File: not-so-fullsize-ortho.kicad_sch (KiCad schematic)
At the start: 10 parts, among them J3 Conn_01x03, J4 Conn_01x04

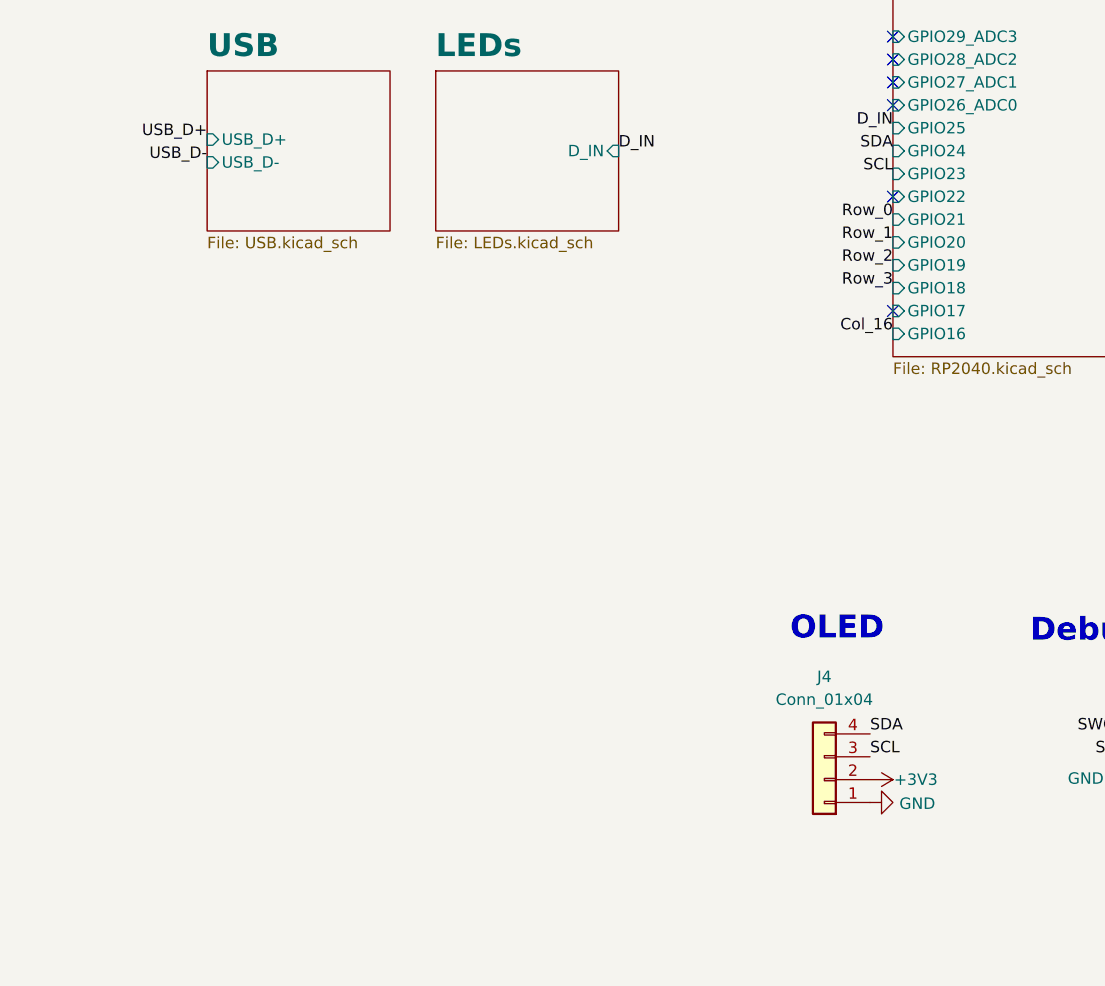
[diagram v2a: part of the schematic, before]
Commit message: remove left most column, reroute rp2040
remove left most column, reroute rp2040 to fit in-between switches, no more oled, last 2 cols (right) are snap off. 
still to do:
- check that the snap cutouts aren't too much,
- add mounting holes for if the side is snapped off.
- still to route columns/rows
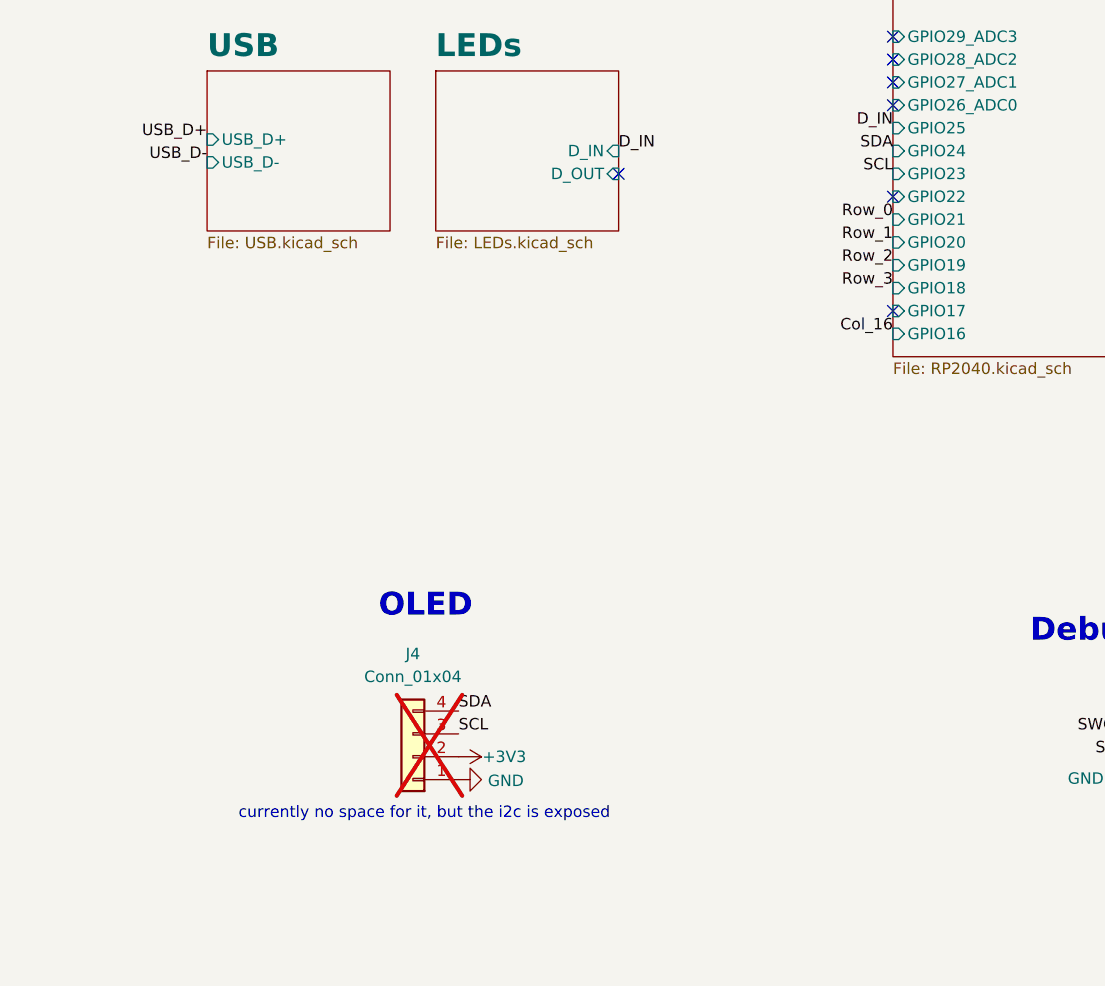
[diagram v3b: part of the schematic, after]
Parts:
- J4: now not fitted
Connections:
- no-connect marks 6 -> 7
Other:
- sheet LEDs ports: added D_OUT; removed none
- note added: "currently no space for it, but the i2c is exposed"
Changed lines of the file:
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@@
+	)
+	(no_connect
+		(at 172.72 151.13)
 	)
 	(no_connect
@@
 		)
 	)
+	(text "currently no space for it, but the i2c is exposed"
+		(exclude_from_sim no)
+		(at 151.13 222.25 0)
+		(effects
+			(font
+				(size 1.27 1.27)
+			)
+		)
+	)
 	(text "OLED"
 		(exclude_from_sim no)
-		(at 191.77 203.2 0)
+		(at 146.05 200.66 0)
 		(effects
 			(font
@@
 	)
 	(label "SCL"
-		(at 200.66 215.9 0)
+		(at 154.94 213.36 0)
 		(fields_autoplaced yes)
 		(effects
@@
 	)
 	(label "SDA"
-		(at 200.66 213.36 0)
+		(at 154.94 210.82 0)
 		(fields_autoplaced yes)
 		(effects
@@
 	(symbol
 		(lib_id "power:GND")
-		(at 200.66 220.98 90)
+		(at 154.94 218.44 90)
 		(mirror x)
 		(unit 1)
@@
 		(dnp no)
 		(property "Reference" "#PWR034"
-			(at 207.01 220.98 0)
+			(at 161.29 218.44 0)
 			(effects
 				(font
@@
 		)
 		(property "Value" "GND"
-			(at 203.9112 221.107 90)
+			(at 158.1912 218.567 90)
 			(effects
 				(font
@@
 		)
 		(property "Footprint" ""
-			(at 200.66 220.98 0)
+			(at 154.94 218.44 0)
 			(effects
 				(font
@@
 		)
 		(property "Datasheet" ""
-			(at 200.66 220.98 0)
+			(at 154.94 218.44 0)
 			(effects
 				(font
@@
 		)
 		(property "Description" ""
-			(at 200.66 220.98 0)
+			(at 154.94 218.44 0)
 			(effects
 				(font
@@
 	(symbol
 		(lib_id "power:+3V3")
-		(at 200.66 218.44 270)
+		(at 154.94 215.9 270)
 		(unit 1)
 		(exclude_from_sim no)
@@
 		(dnp no)
 		(property "Reference" "#PWR035"
-			(at 196.85 218.44 0)
+			(at 151.13 215.9 0)
 			(effects
 				(font
@@
 		)
 		(property "Value" "+3V3"
-			(at 205.74 218.44 90)
+			(at 160.02 215.9 90)
 			(effects
 				(font
@@
 		)
 		(property "Footprint" ""
-			(at 200.66 218.44 0)
+			(at 154.94 215.9 0)
 			(effects
 				(font
@@
 		)
 		(property "Datasheet" ""
-			(at 200.66 218.44 0)
+			(at 154.94 215.9 0)
 			(effects
 				(font
@@
 		)
 		(property "Description" ""
-			(at 200.66 218.44 0)
+			(at 154.94 215.9 0)
 			(effects
 				(font
@@
 	(symbol
 		(lib_id "Connector_Generic:Conn_01x04")
-		(at 195.58 218.44 180)
+		(at 149.86 215.9 180)
 		(unit 1)
 		(exclude_from_sim no)
 		(in_bom yes)
 		(on_board yes)
-		(dnp no)
+		(dnp yes)
 		(fields_autoplaced yes)
 		(property "Reference" "J4"
-			(at 195.58 207.01 0)
+			(at 149.86 204.47 0)
 			(effects
 				(font
@@
 		)
 		(property "Value" "Conn_01x04"
-			(at 195.58 209.55 0)
+			(at 149.86 207.01 0)
 			(effects
 				(font
@@
 		)
 		(property "Footprint" "Connector_PinSocket_2.54mm:PinSocket_1x04_P2.54mm_Vertical"
-			(at 195.58 218.44 0)
+			(at 149.86 215.9 0)
 			(effects
 				(font
@@
 		)
 		(property "Datasheet" "~"
-			(at 195.58 218.44 0)
+			(at 149.86 215.9 0)
 			(effects
 				(font
@@
 		)
 		(property "Description" "Generic connector, single row, 01x04, script generated (kicad-library-utils/schlib/autogen/connector/)"
-			(at 195.58 218.44 0)
+			(at 149.86 215.9 0)
 			(effects
 				(font
@@
 			(effects
 				(font
+					(size 1.27 1.27)
+				)
+				(justify right)
+			)
+		)
+		(pin "D_OUT" input
+			(at 172.72 151.13 0)
+			(effects
+				(font

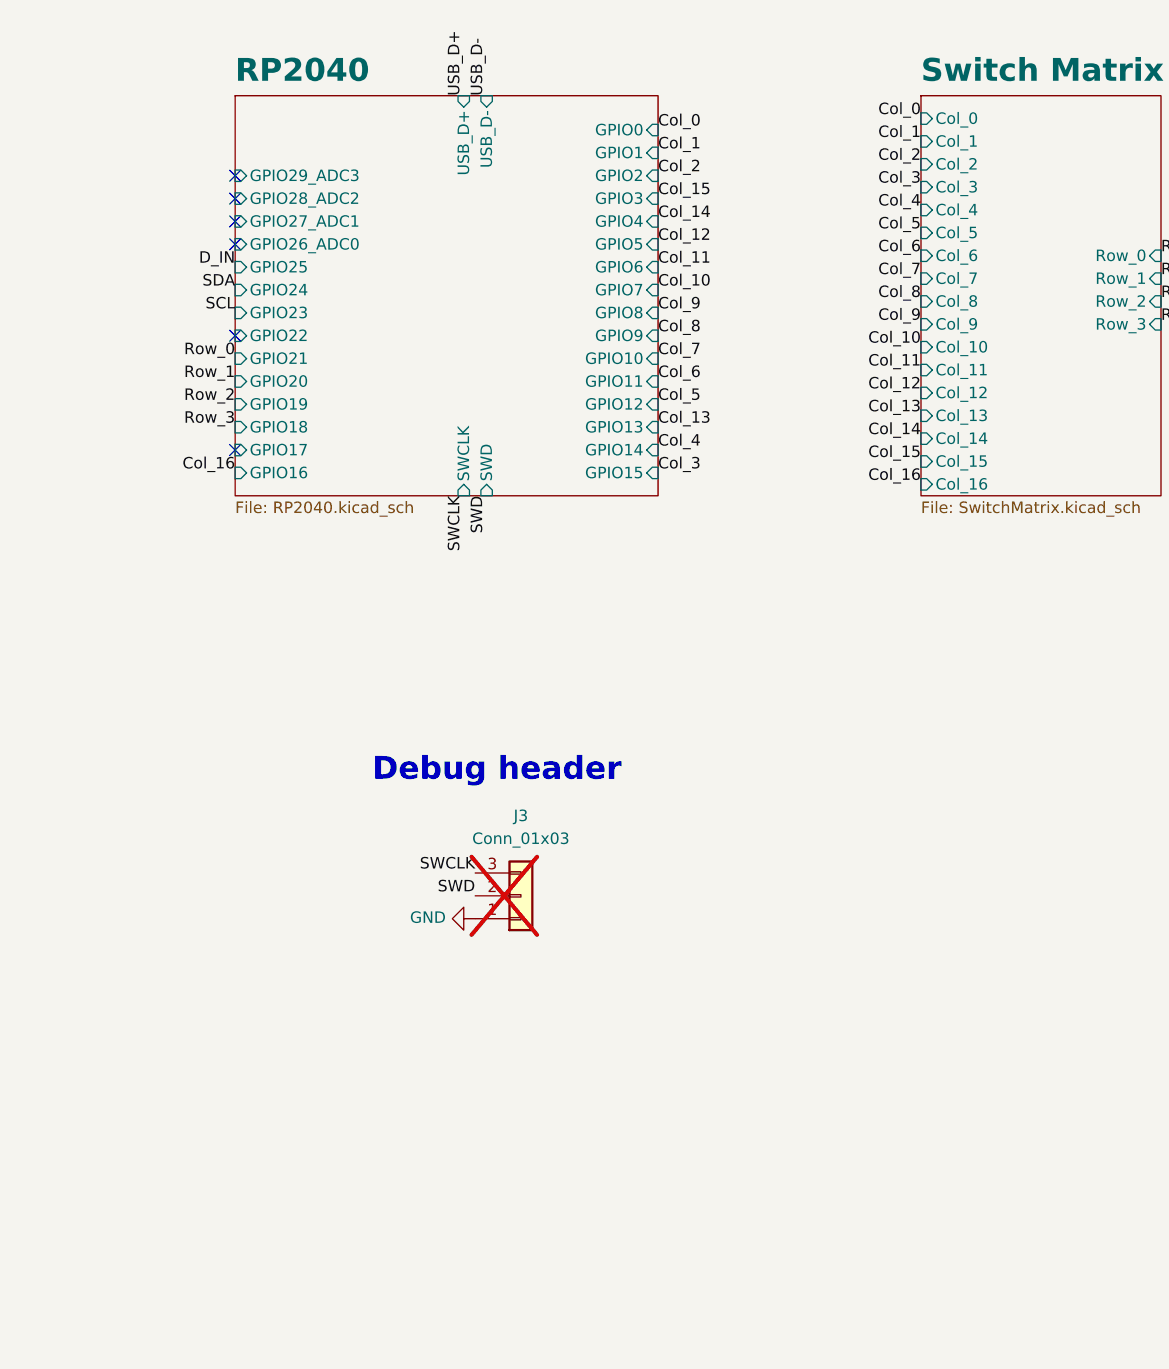
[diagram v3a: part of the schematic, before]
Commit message: routing, rotate leds to make tracks easier
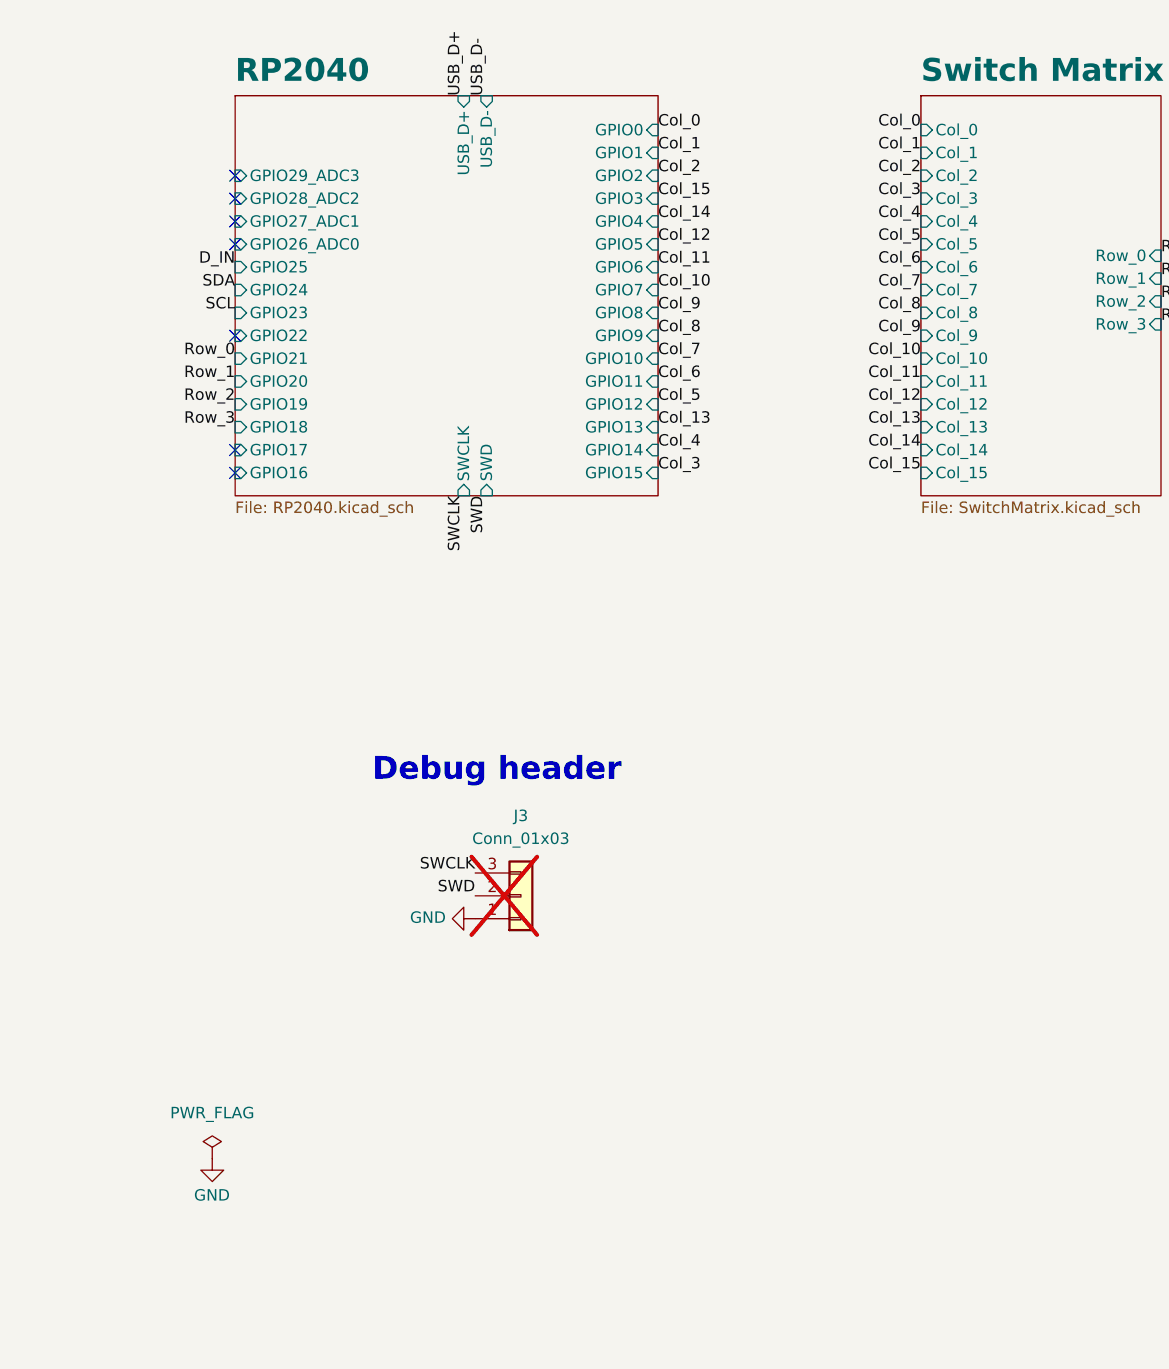
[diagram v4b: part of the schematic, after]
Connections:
- no-connect marks 7 -> 8
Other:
- sheet Switch Matrix ports: added none; removed Col_16
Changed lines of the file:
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@@
+	)
+	(no_connect
+		(at 203.2 168.91)
 	)
 	(no_connect
@@
 	)
 	(label "Col_7"
-		(at 279.4 147.32 180)
-		(fields_autoplaced yes)
-		(effects
-			(font
-				(size 1.27 1.27)
-			)
-			(justify right bottom)
-		)
-	)
-	(label "Col_16"
-		(at 279.4 170.18 180)
+		(at 279.4 148.59 180)
 		(fields_autoplaced yes)
 		(effects
@@
 	)
 	(label "Col_6"
-		(at 279.4 144.78 180)
+		(at 279.4 146.05 180)
 		(fields_autoplaced yes)
 		(effects
@@
 		)
 	)
-	(label "Col_16"
-		(at 203.2 168.91 180)
-		(fields_autoplaced yes)
-		(effects
-			(font
-				(size 1.27 1.27)
-			)
-			(justify right bottom)
-		)
-	)
 	(label "Col_2"
 		(at 250.19 135.89 0)
@@
 	)
 	(label "Col_5"
-		(at 279.4 142.24 180)
+		(at 279.4 143.51 180)
 		(fields_autoplaced yes)
 		(effects
@@
 	)
 	(label "Col_0"
-		(at 279.4 129.54 180)
+		(at 279.4 130.81 180)
 		(fields_autoplaced yes)
 		(effects
@@
 	)
 	(label "Col_4"
-		(at 279.4 139.7 180)
+		(at 279.4 140.97 180)
 		(fields_autoplaced yes)
 		(effects
@@
 	)
 	(label "Col_1"
-		(at 279.4 132.08 180)
+		(at 279.4 133.35 180)
 		(fields_autoplaced yes)
 		(effects
@@
 	)
 	(label "Col_13"
-		(at 279.4 162.56 180)
+		(at 279.4 163.83 180)
 		(fields_autoplaced yes)
 		(effects
@@
 	)
 	(label "Col_15"
-		(at 279.4 167.64 180)
+		(at 279.4 168.91 180)
 		(fields_autoplaced yes)
 		(effects
@@
 	)
 	(label "Col_3"
-		(at 279.4 137.16 180)
+		(at 279.4 138.43 180)
 		(fields_autoplaced yes)
 		(effects
@@
 	)
 	(label "Col_14"
-		(at 279.4 165.1 180)
+		(at 279.4 166.37 180)
 		(fields_autoplaced yes)
 		(effects
@@
 	)
 	(label "Col_9"
-		(at 279.4 152.4 180)
+		(at 279.4 153.67 180)
 		(fields_autoplaced yes)
 		(effects
@@
 	)
 	(label "Col_10"
-		(at 279.4 154.94 180)
+		(at 279.4 156.21 180)
 		(fields_autoplaced yes)
 		(effects
@@
 	)
 	(label "Col_11"
-		(at 279.4 157.48 180)
+		(at 279.4 158.75 180)
 		(fields_autoplaced yes)
 		(effects
@@
 	)
 	(label "Col_8"
-		(at 279.4 149.86 180)
+		(at 279.4 151.13 180)
 		(fields_autoplaced yes)
 		(effects
@@
 	)
 	(label "Col_12"
-		(at 279.4 160.02 180)
+		(at 279.4 161.29 180)
 		(fields_autoplaced yes)
 		(effects
@@
 	)
 	(label "Col_2"
-		(at 279.4 134.62 180)
+		(at 279.4 135.89 180)
 		(fields_autoplaced yes)
 		(effects
@@
 				(path "/e63e39d7-6ac0-4ffd-8aa3-1841a4541b55"
 					(reference "H6")
+					(unit 1)
+				)
+			)
+		)
+	)
+	(symbol
+		(lib_id "PCM_4ms_Power-symbol:PWR_FLAG")
+		(at 200.66 245.11 0)
+		(unit 1)
+		(exclude_from_sim no)
+		(in_bom yes)
+		(on_board yes)
+		(dnp no)
+		(fields_autoplaced yes)
+		(property "Reference" "#FLG02"
+			(at 200.66 243.205 0)
+			(effects
+				(font
+					(size 1.27 1.27)
+				)
+				(hide yes)
+			)
+		)
+		(property "Value" "PWR_FLAG"
+			(at 200.66 240.03 0)
+			(effects
+				(font
+					(size 1.27 1.27)
+				)
+			)
+		)
+		(property "Footprint" ""
+			(at 200.66 245.11 0)
+			(effects
+				(font
+					(size 1.27 1.27)
+				)
+				(hide yes)
+			)
+		)
+		(property "Datasheet" ""
+			(at 200.66 245.11 0)
+			(effects
+				(font
+					(size 1.27 1.27)
+				)
+				(hide yes)
+			)
+		)
+		(property "Description" ""
+			(at 200.66 245.11 0)
+			(effects
+				(font
+					(size 1.27 1.27)
+				)
+				(hide yes)
+			)
+		)
+		(pin "1"
+		)
+		(instances
+			(project ""
+				(path "/e63e39d7-6ac0-4ffd-8aa3-1841a4541b55"
+					(reference "#FLG02")
 					(unit 1)
 				)
@@
 			)
 		)
-		(property "Description" ""
+		(property "Description" "Power symbol creates a global label with name \"GND\" , ground"
 			(at 154.94 218.44 0)
 			(effects
@@
 			)
 		)
-		(property "Description" ""
+		(property "Description" "Power symbol creates a global label with name \"+3V3\""
 			(at 154.94 215.9 0)
 			(effects
@@
 			)
 		)
-		(property "Description" ""
+		(property "Description" "Power symbol creates a global label with name \"GND\" , ground"
 			(at 229.87 218.44 0)
 			(effects
@@
 	)
 	(symbol
+		(lib_id "power:GND")
+		(at 200.66 245.11 0)
+		(mirror y)
+		(unit 1)
+		(exclude_from_sim no)
+		(in_bom yes)
+		(on_board yes)
+		(dnp no)
+		(property "Reference" "#PWR047"
+			(at 200.66 251.46 0)
+			(effects
+				(font
+					(size 1.27 1.27)
+				)
+				(hide yes)
+			)
+		)
+		(property "Value" "GND"
+			(at 198.628 249.174 0)
+			(effects
+				(font
+					(size 1.27 1.27)
+				)
+				(justify right)
+			)
+		)
+		(property "Footprint" ""
+			(at 200.66 245.11 0)
+			(effects
+				(font
+					(size 1.27 1.27)
+				)
+				(hide yes)
+			)
+		)
+		(property "Datasheet" ""
+			(at 200.66 245.11 0)
+			(effects
+				(font
+					(size 1.27 1.27)
+				)
+				(hide yes)
+			)
+		)
+		(property "Description" "Power symbol creates a global label with name \"GND\" , ground"
+			(at 200.66 245.11 0)
+			(effects
+				(font
+					(size 1.27 1.27)
+				)
+				(hide yes)
+			)
+		)
+		(pin "1"
+		)
+		(instances
+			(project "not-so-fullsize-ortho"
+				(path "/e63e39d7-6ac0-4ffd-8aa3-1841a4541b55"
+					(reference "#PWR047")
+					(unit 1)
+				)
+			)
+		)
+	)
+	(symbol
 		(lib_id "Connector_Generic:Conn_01x03")
 		(at 234.95 215.9 0)
@@
 		)
 		(pin "Col_13" input
-			(at 279.4 162.56 180)
+			(at 279.4 163.83 180)
 			(effects
 				(font
@@
 		)
 		(pin "Col_9" input
-			(at 279.4 152.4 180)
+			(at 279.4 153.67 180)
 			(effects
 				(font
@@
 		)
 		(pin "Col_11" input
-			(at 279.4 157.48 180)
+			(at 279.4 158.75 180)
 			(effects
 				(font
@@
 		)
 		(pin "Col_8" input
-			(at 279.4 149.86 180)
+			(at 279.4 151.13 180)
 			(effects
 				(font
@@
 		)
 		(pin "Col_12" input
-			(at 279.4 160.02 180)
+			(at 279.4 161.29 180)
 			(effects
 				(font
@@
 		)
 		(pin "Col_10" input
-			(at 279.4 154.94 180)
+			(at 279.4 156.21 180)
 			(effects
 				(font
@@
 		)
 		(pin "Col_14" input
-			(at 279.4 165.1 180)
+			(at 279.4 166.37 180)
 			(effects
 				(font
@@
 		)
 		(pin "Col_6" input
-			(at 279.4 144.78 180)
+			(at 279.4 146.05 180)
 			(effects
 				(font
@@
 		)
 		(pin "Col_5" input
-			(at 279.4 142.24 180)
+			(at 279.4 143.51 180)
 			(effects
 				(font
@@
 		)
 		(pin "Col_7" input
-			(at 279.4 147.32 180)
+			(at 279.4 148.59 180)
 			(effects
 				(font
@@
 		)
 		(pin "Col_3" input
-			(at 279.4 137.16 180)
+			(at 279.4 138.43 180)
 			(effects
 				(font
@@
 		)
 		(pin "Col_0" input
-			(at 279.4 129.54 180)
+			(at 279.4 130.81 180)
 			(effects
 				(font
@@
 		)
 		(pin "Col_2" input
-			(at 279.4 134.62 180)
+			(at 279.4 135.89 180)
 			(effects
 				(font
@@
 		)
 		(pin "Col_1" input
-			(at 279.4 132.08 180)
+			(at 279.4 133.35 180)
 			(effects
 				(font
@@
 		)
 		(pin "Col_15" input
-			(at 279.4 167.64 180)
-			(effects
-				(font
-					(size 1.27 1.27)
-				)
-				(justify left)
-			)
-		)
-		(pin "Col_16" input
-			(at 279.4 170.18 180)
+			(at 279.4 168.91 180)
 			(effects
 				(font
@@
 		)
 		(pin "Col_4" input
-			(at 279.4 139.7 180)
-			(effects
-				(font
+			(at 279.4 140.97 180)
+			(effects
+				(font

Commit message: pretty much done
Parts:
- J4: footprint Connector_PinSocket_2.54mm:PinSocket_1x04_P2.54mm_Vertical -> Connector_PinHeader_2.54mm:PinHeader_1x04_P2.54mm_Vertical
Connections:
- net SWCLK: now also J3.2 (Pin_2); no longer J3.3 (Pin_3)
- net SWD: now also J3.3 (Pin_3); no longer J3.2 (Pin_2)
